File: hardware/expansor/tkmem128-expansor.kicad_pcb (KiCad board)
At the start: 2 copper layers, 78.7 x 45 mm, 3 parts, among them J1 Terminais do conector, J2 Passagem

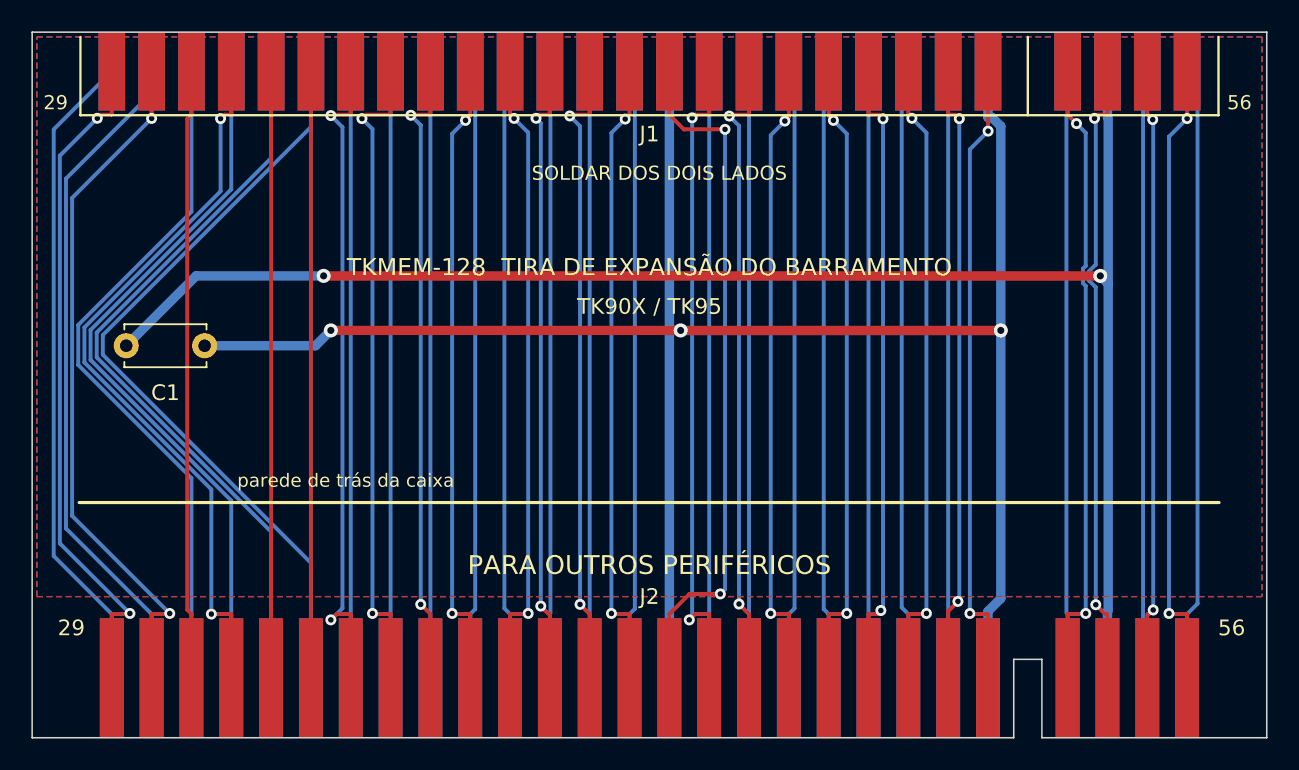
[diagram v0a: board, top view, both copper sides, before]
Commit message: Rasgo da guia 2 mm mais fundo e serigrafia em negrito
Conferencia em papel do Leonardo (impressao 1:1 contra as pecas reais, jul/2026):
todas as medidas e alinhamentos bateram. Uma correcao saiu dela.

RASGO DA GUIA (tira, entre os dedos de J2): 5,0 -> 7,0 mm de profundidade. Os
5 mm nao chegavam ao fundo da guia do conector. Agora vai de y=45,00 a y=38,00.

  folga lateral ate o cobre mais proximo (pinos 4/6/51/53)   0,88 mm
  quanto ainda daria para aprofundar                         0,62 mm

Esses 0,62 mm sao o limite: os dedos comecam em y=37,38. Passar disso obriga a
encurta-los tambem. Anotado no item 3 de ANTES-DE-FABRICAR.

A profundidade virou parametro (KEYSLOT_DEPTH em netlist_exp.py) em vez de
numero solto no gen_pcb.py, e ganhou tools/ajusta_guia.py para aplicar numa
placa ja roteada — refaz o contorno e repreenche as zonas.

O primeiro recorte deixou orfao o fundo do rasgo antigo: um traco de Edge.Cuts
solto no meio da placa, que nenhum DRC acusa e o fabricante cortaria. Filtrar
tracos por posicao e fragil, entao ajusta_guia.py reconstroi o contorno inteiro
e verifica que ele fecha (cada vertice usado por exatamente dois tracos).

NEGRITO: o Leonardo pos a serigrafia da principal em negrito, para ler melhor.
Faltavam 9 referencias (C1..C6, D1, TP1, TP2) e a tira inteira. Uniformizado
nas duas placas com tools/silk_negrito.py, que segue a regra do proprio KiCad —
espessura = 0,2 x o tamanho da fonte, e nao um valor fixo, que e o que mantem
texto grande e pequeno com o mesmo peso.

Tambem: *.lck no .gitignore e os dois que tinham entrado no repositorio
removidos do indice.

DRC: principal 2 violacoes (as starved_thermal de sempre), tira 0. Alinhamento
entre as placas inalterado.

Co-Authored-By: Claude Opus 5 <noreply@anthropic.com>
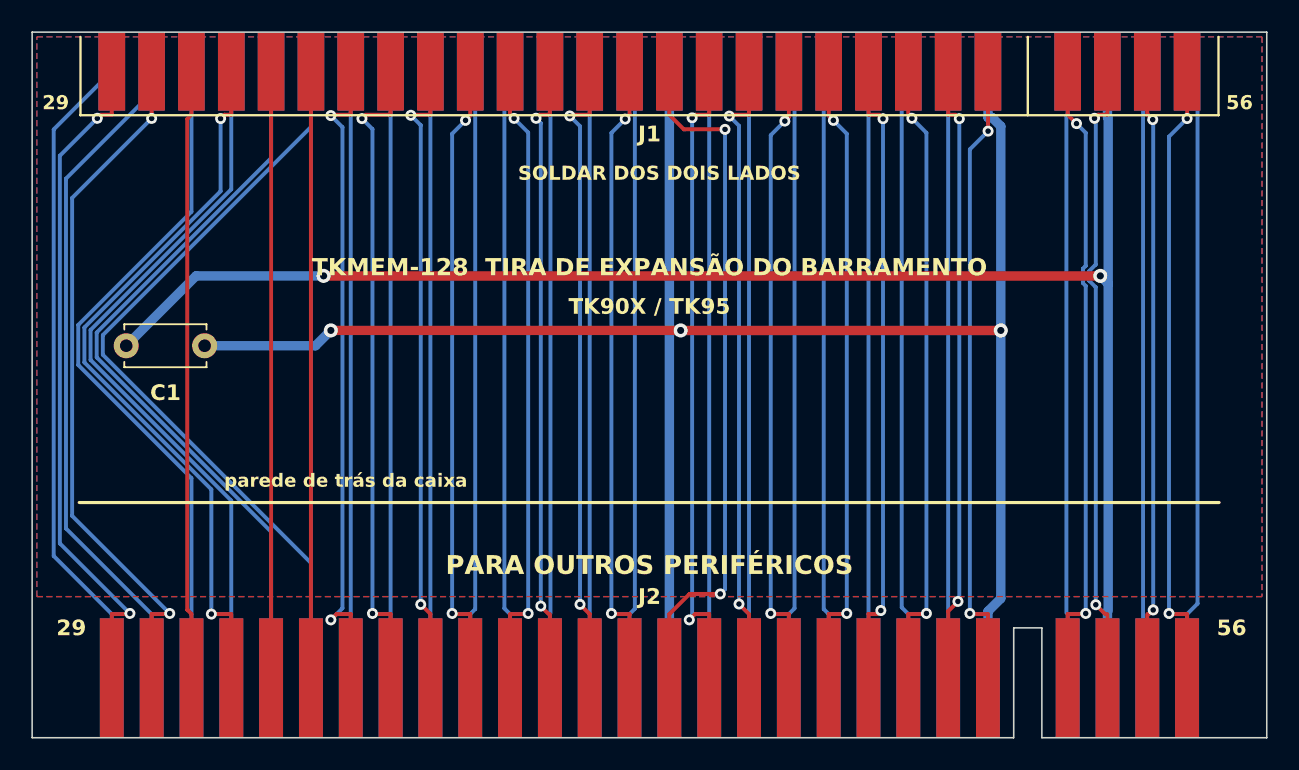
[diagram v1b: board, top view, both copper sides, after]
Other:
- outline, holes or cut-outs redrawn
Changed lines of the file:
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@@
 				(font
 					(size 1 1)
-					(thickness 0.15)
+					(thickness 0.2)
+					(bold yes)
 				)
 			)
@@
 				(font
 					(size 1 1)
-					(thickness 0.15)
+					(thickness 0.2)
+					(bold yes)
 				)
 			)
@@
 				(font
 					(size 1 1)
-					(thickness 0.15)
+					(thickness 0.2)
+					(bold yes)
 				)
 			)
@@
 				(font
 					(size 1 1)
-					(thickness 0.15)
+					(thickness 0.2)
+					(bold yes)
 				)
 				(justify mirror)
@@
 				(font
 					(size 1 1)
-					(thickness 0.15)
+					(thickness 0.2)
+					(bold yes)
 				)
 				(justify mirror)
@@
 				(font
 					(size 1 1)
-					(thickness 0.15)
+					(thickness 0.2)
+					(bold yes)
 				)
 			)
@@
 				(font
 					(size 0.9 0.9)
-					(thickness 0.15)
+					(thickness 0.18)
+					(bold yes)
 				)
 			)
@@
 				(font
 					(size 0.9 0.9)
-					(thickness 0.15)
+					(thickness 0.18)
+					(bold yes)
 				)
 			)
@@
 				(font
 					(size 0.9 0.9)
-					(thickness 0.15)
+					(thickness 0.18)
+					(bold yes)
 				)
 			)
@@
 				(font
 					(size 0.9 0.9)
-					(thickness 0.15)
+					(thickness 0.18)
+					(bold yes)
 				)
 				(justify mirror)
@@
 				(font
 					(size 0.9 0.9)
-					(thickness 0.15)
+					(thickness 0.18)
+					(bold yes)
 				)
 				(justify mirror)
@@
 				(font
 					(size 0.9 0.9)
-					(thickness 0.15)
+					(thickness 0.18)
+					(bold yes)
 				)
 				(justify mirror)
@@
 				(font
 					(size 1 1)
-					(thickness 0.15)
+					(thickness 0.2)
+					(bold yes)
 				)
 			)
@@
 	)
 	(gr_line
-		(start 62.6 40)
-		(end 64.4 40)
+		(start 62.6 38)
+		(end 64.4 38)
 		(stroke
 			(width 0.1)
@@
 	(gr_line
 		(start 62.6 45)
-		(end 62.6 40)
+		(end 62.6 38)
 		(stroke
 			(width 0.1)
@@
 	)
 	(gr_line
-		(start 64.4 40)
+		(start 64.4 38)
 		(end 64.4 45)
 		(stroke
@@
 			(font
 				(size 0.85 0.85)
-				(thickness 0.15)
+				(thickness 0.17)
+				(bold yes)
 			)
 		)
@@
 			(font
 				(size 1 1)
-				(thickness 0.15)
+				(thickness 0.2)
+				(bold yes)
 			)
 		)
@@
 			(font
 				(size 1.1 1.1)
-				(thickness 0.15)
+				(thickness 0.22)
+				(bold yes)
 			)
 		)
@@
 			(font
 				(size 1.2 1.2)
-				(thickness 0.15)
+				(thickness 0.24)
+				(bold yes)
 			)
 		)
@@
 			(font
 				(size 0.9 0.9)
-				(thickness 0.15)
+				(thickness 0.18)
+				(bold yes)
 			)
 			(justify mirror)
@@
 			(font
 				(size 0.9 0.9)
-				(thickness 0.15)
+				(thickness 0.18)
+				(bold yes)
 			)
 			(justify mirror)

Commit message: Tira: 54 retas de 1,5 mm, zero via, zero plano de terra
Voce esta certo nas tres criticas. Medindo o que estava la:

  trilha de sinal      0,25 mm
  cobre por face       B.Cu 1885 mm  x  F.Cu 423 mm   (82% numa face so)
  vias                 53

Numa placa que alimenta uma cascata de perifericos isso e indefensavel. E o pior
e que a tira nem tem problema de roteamento: J1 e J2 estao nas MESMAS colunas e
cada pino fica na MESMA face nos dois (F.Cu = 29..56, B.Cu = 1..28). Cada rede e
uma reta vertical de x constante. Nao existe um unico cruzamento na placa. O
Freerouting nao sabia disso e inventou 53 vias.

Refeito a mao, sem autorouter:

  54 trilhas retas de 1,5 mm
  0 vias
  F.Cu 1044,6 mm  x  B.Cu 1044,6 mm   (simetrico ao milimetro)

1,5 mm e a largura maxima limpa: os dedos de J2 tem 1,524 mm e o passo e 2,54,
sobrando 1,04 mm de vao entre vizinhas. Suporta ~3,5 A contra ~0,9 A antes.

Plano de terra removido, como voce pediu. Com as verticais ocupando as duas
faces inteiras, o plano so existia em fiapos de 1 mm entre trilhas — inutil como
retorno, util so para criar acoplamento.

C1 SAIU, e por um motivo estrutural que vale registrar: numa placa de passagem
com ilhas presas a uma face, cada COLUNA carrega redes diferentes nas duas
faces. Em x=68,58, B.Cu e +5V e F.Cu e D7. Entao QUALQUER ilha passante fora da
coluna da guia e um curto entre duas redes. C1 era THT. E nem em SMD caberia:
BUS_9V (x=66,04) fica entre o +5V (68,58) e o GND mais proximo (60,96), com as
duas faces ocupadas — nao ha caminho de 2 camadas de um ao outro. O
desacoplamento fica na principal (5x100n + 10u) e no periferico seguinte.

Entrou W1, o link de terra: os pinos 6 e 14 sao os dois GND do barramento, e
liga-los exigiria cruzar 7 colunas. Duas ilhas SMD em B.Cu e um fio isolado por
cima resolvem — e e o retorno de terra de tudo que vier em cascata. Footprint
board_only: fio e ligacao de cobre, nao componente, entao nao tem simbolo nem
entra na lista de material.

DRC 0 violacoes. O 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
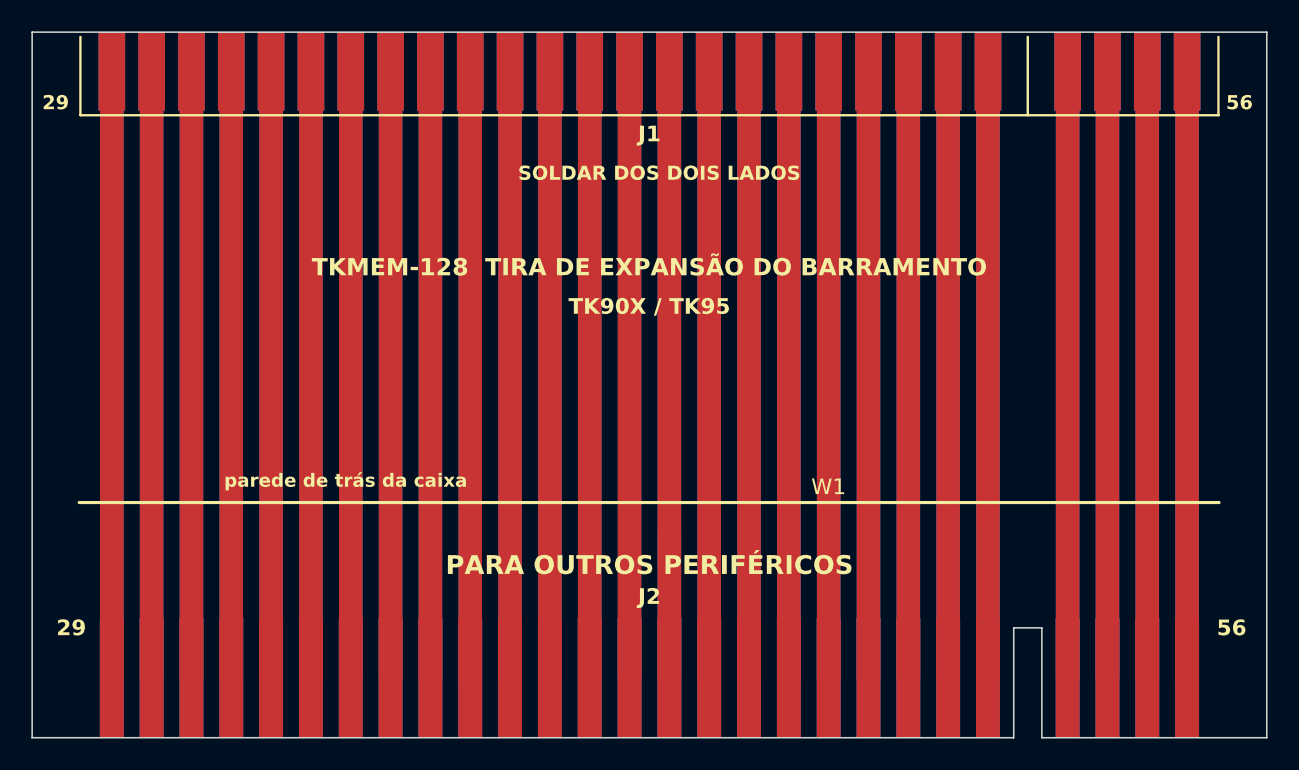
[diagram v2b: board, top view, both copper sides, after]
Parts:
- removed C1: 100n, C_Disc_D5.0mm_W2.5mm_P5.00mm
- added W1: WireLink_GND_P20.32mm, WireLink_GND_P20.32mm, F.Cu at (50.8, 33.0)
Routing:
- net +5V: track 103.3 -> 38.7 mm, vias 2 -> 0
- net GND: track 130.1 -> 77.4 mm, vias 3 -> 0
- net A5: track 49.7 -> 38.7 mm
- net A4: track 47.9 -> 38.7 mm
- net BUS_RFSH: track 47.4 -> 38.7 mm, vias 2 -> 0
- net ROMCS_BUS: track 46.1 -> 38.7 mm
- net BUS_BUSACK: track 44.7 -> 38.7 mm
- net A10: track 44.4 -> 38.7 mm, vias 2 -> 0
- net BUS_NMI: track 44.3 -> 38.7 mm, vias 2 -> 0
- net BUS_P29: track 43.4 -> 38.7 mm, vias 2 -> 0
- net A9: track 43.2 -> 38.7 mm
- net BUS_P35: track 42.3 -> 38.7 mm, vias 2 -> 0
- net A11: track 41.8 -> 38.7 mm
- net BUS_WAIT: track 41.7 -> 38.7 mm, vias 2 -> 0
- net BUS_INT: track 41.5 -> 38.7 mm, vias 2 -> 0
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- removed copper zone on B.Cu, net GND
- removed copper zone on F.Cu, net GND
